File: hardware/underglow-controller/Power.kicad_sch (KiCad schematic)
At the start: 17 parts, among them Q6 Q_PMOS_GDS, U8 ADP2303ARDZ-3.3

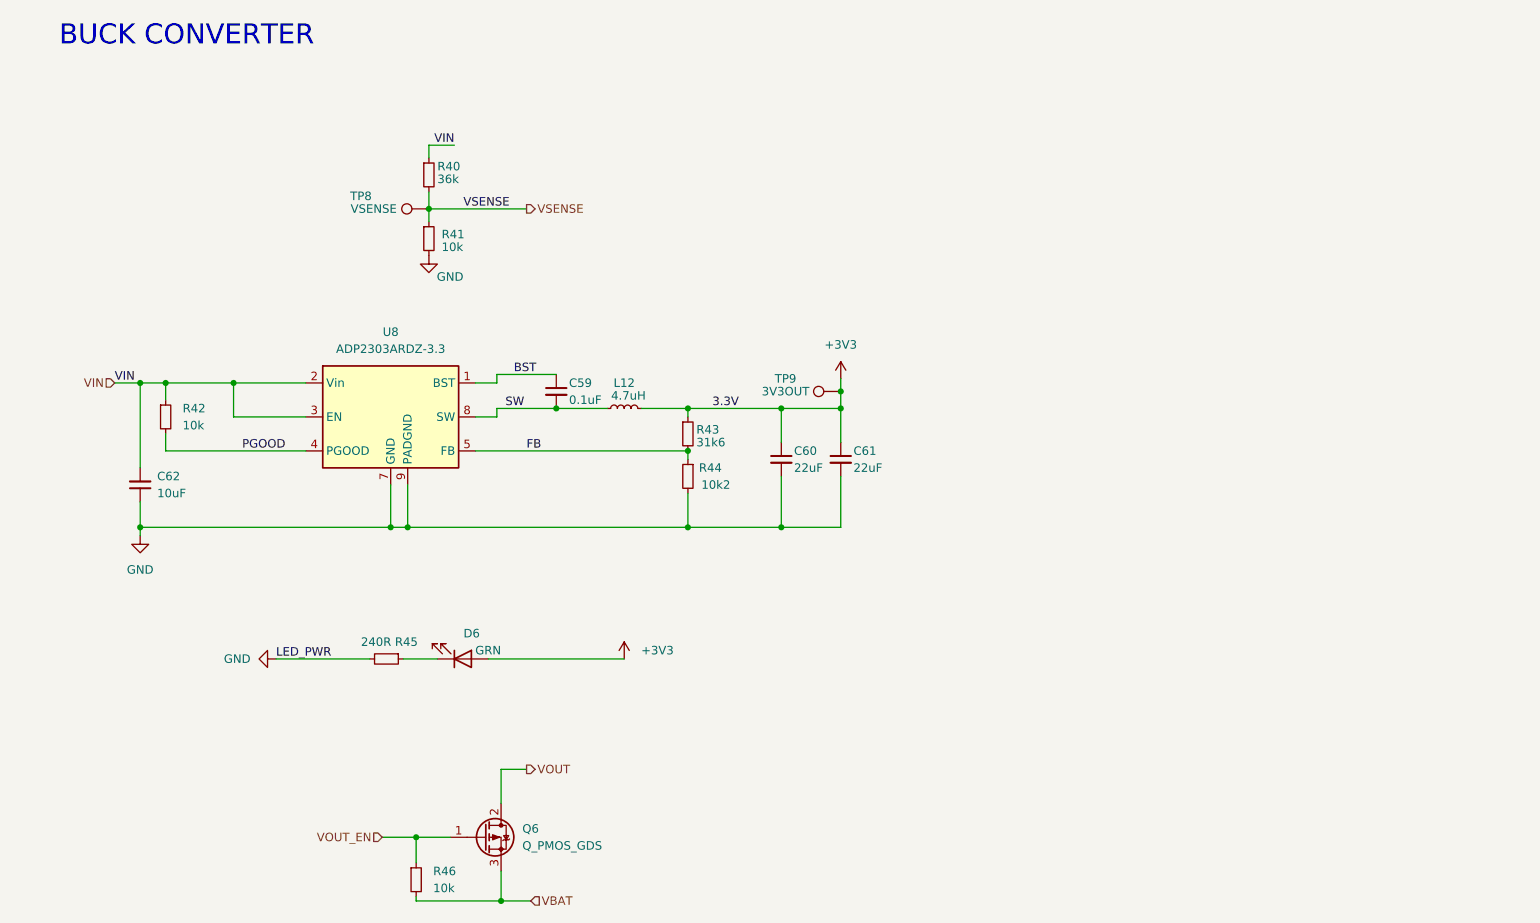
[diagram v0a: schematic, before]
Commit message: replace pmic
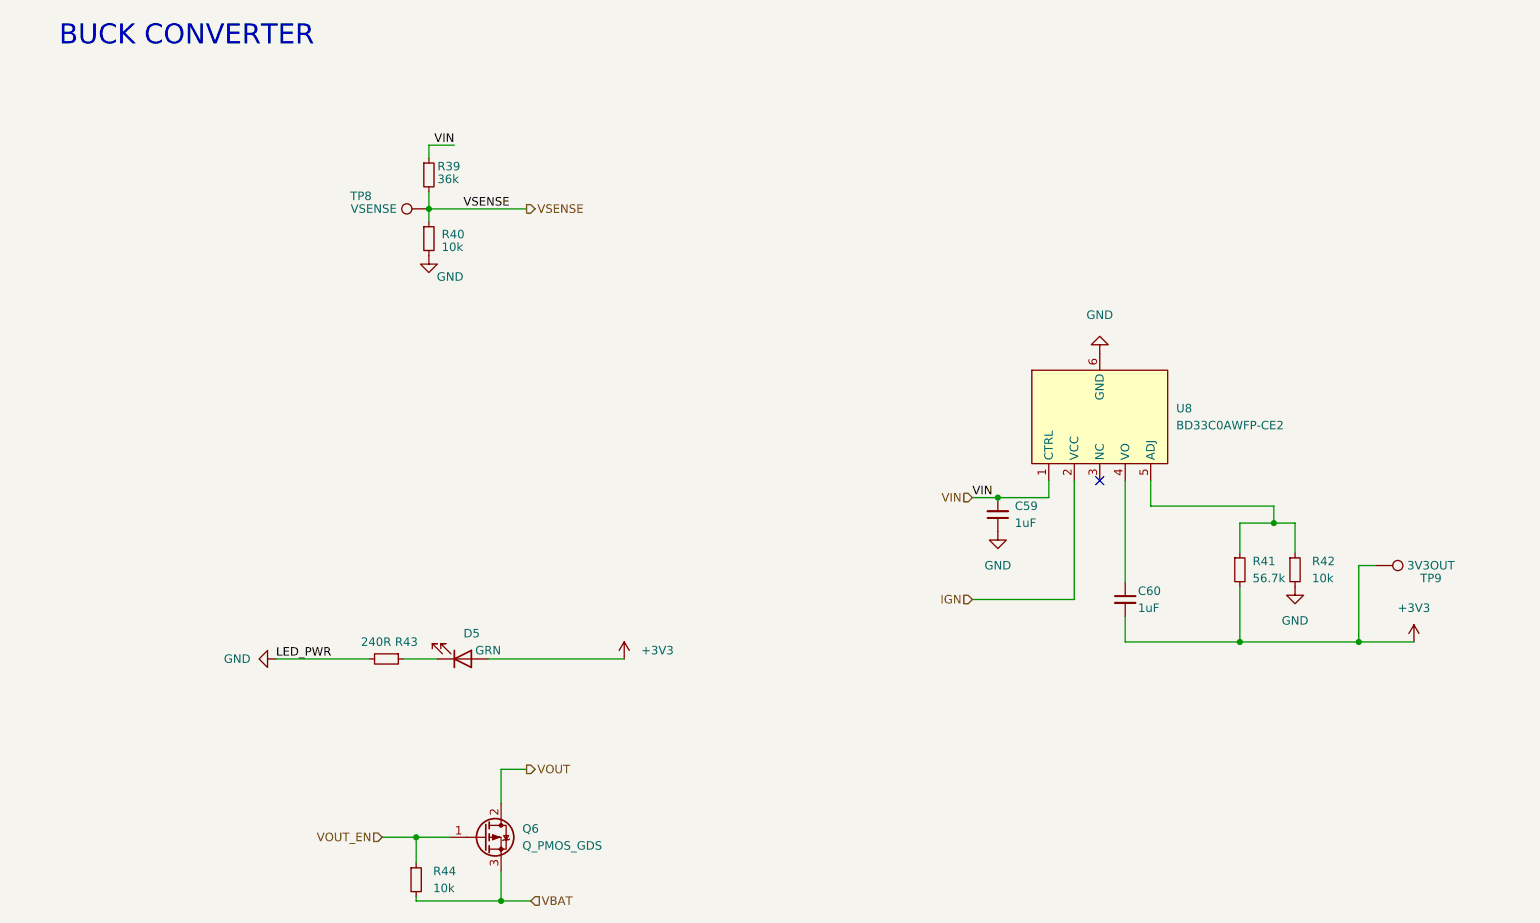
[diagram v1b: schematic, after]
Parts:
- removed C59: 0.1uF, Capacitor_SMD:C_0805_2012Metric, symbol Device:C_Small
- removed C61: 22uF, Capacitor_SMD:C_0805_2012Metric, symbol Device:C_Small
- removed L12: 4.7uH, Inductor_SMD:L_Bourns-SRN6028, symbol Device:L_Small
- removed R43: 31k6, Resistor_SMD:R_0603_1608Metric, symbol Device:R_Small
- removed R44: 10k2, Resistor_SMD:R_0603_1608Metric, symbol Device:R_Small
- removed U8: ADP2303ARDZ-3.3, Package_SO:SOIC-8-1EP_3.9x4.9mm_P1.27mm_EP2.29x3mm_ThermalVias, symbol Regulator_Switching:ADP2303ARDZ-3.3
- added R41: 56.7k, Resistor_SMD:R_0805_2012Metric, symbol Device:R_Small
- added U8: BD33C0AWFP-CE2, Package_TO_SOT_SMD:TO-252-5_TabPin6, symbol ConeCodes:BD33C0AWFP-CE2
- C59: renamed from C62; value 10uF -> 1uF; MPN CL21A106KAFN3NE -> (none)
- C60: value 22uF -> 1uF; MPN CL21A226MOQNNNE -> (none)
- R42: footprint Resistor_SMD:R_0603_1608Metric -> Resistor_SMD:R_0805_2012Metric; MPN RNCP0603FTD10K0 -> (none)
- renumbered D6 to D5, R40 to R39, R41 to R40, R45 to R43, R46 to R44
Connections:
- net PGOOD is gone; now on net GND: R42.2
- net +3V3: now also C60.2, R41.2; no longer C60.1
- net GND: now also U8.6 (GND); no longer C60.2
- net VIN: now also U8.1 (CTRL); no longer R42.1
- new net: R41.1, R42.1, U8.5 (ADJ)
- new net: C60.1, U8.4 (VO)
- new net IGN: U8.2 (VCC)
- no-connect marks 0 -> 1
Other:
- moved on the sheet: C59, TP9

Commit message: iasdf
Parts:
- removed Q6: Q_PMOS_GDS, Package_TO_SOT_SMD:TO-252-2, symbol Device:Q_PMOS_GDS
- removed R44: 10k, Resistor_SMD:R_0603_1608Metric, symbol Device:R_Small
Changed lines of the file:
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@@
   (junction (at 198.755 92.075) (diameter 0) (color 0 0 0 0)
-  )
-  (junction (at 70.485 139.065) (diameter 0) (color 0 0 0 0)
-  )
-  (junction (at 83.185 148.59) (diameter 0) (color 0 0 0 0)
   )
   (junction (at 193.675 109.855) (diameter 0) (color 0 0 0 0)
@@
     (stroke (width 0) (type default) (color 0 0 0 0))
   )
-  (wire (pts (xy 87.63 148.59) (xy 83.185 148.59))
-    (stroke (width 0) (type default) (color 0 0 0 0))
-  )
   (wire (pts (xy 176.53 109.855) (xy 176.53 106.045))
     (stroke (width 0) (type default) (color 0 0 0 0))
   )
-  (wire (pts (xy 83.185 148.59) (xy 83.185 144.145))
-    (stroke (width 0) (type default) (color 0 0 0 0))
-  )
-  (wire (pts (xy 70.485 139.065) (xy 70.485 142.875))
-    (stroke (width 0) (type default) (color 0 0 0 0))
-  )
   (wire (pts (xy 213.995 98.425) (xy 211.455 98.425))
     (stroke (width 0) (type default) (color 0 0 0 0))
@@
     (stroke (width 0) (type default) (color 0 0 0 0))
   )
-  (wire (pts (xy 65.405 139.065) (xy 70.485 139.065))
-    (stroke (width 0) (type default) (color 0 0 0 0))
-  )
   (wire (pts (xy 193.675 92.075) (xy 198.755 92.075))
     (stroke (width 0) (type default) (color 0 0 0 0))
@@
     (stroke (width 0) (type default) (color 0 0 0 0))
   )
-  (wire (pts (xy 70.485 139.065) (xy 75.565 139.065))
-    (stroke (width 0) (type default) (color 0 0 0 0))
-  )
   (wire (pts (xy 176.53 85.725) (xy 176.53 100.965))
     (stroke (width 0) (type default) (color 0 0 0 0))
@@
     (stroke (width 0) (type default) (color 0 0 0 0))
   )
-  (wire (pts (xy 83.185 128.905) (xy 83.185 133.985))
-    (stroke (width 0) (type default) (color 0 0 0 0))
-  )
   (wire (pts (xy 211.455 98.425) (xy 211.455 109.855))
     (stroke (width 0) (type default) (color 0 0 0 0))
@@
     (stroke (width 0) (type default) (color 0 0 0 0))
   )
-  (wire (pts (xy 70.485 148.59) (xy 70.485 147.955))
-    (stroke (width 0) (type default) (color 0 0 0 0))
-  )
-  (wire (pts (xy 83.185 148.59) (xy 70.485 148.59))
-    (stroke (width 0) (type default) (color 0 0 0 0))
-  )
   (wire (pts (xy 180.34 85.725) (xy 180.34 89.535))
-    (stroke (width 0) (type default) (color 0 0 0 0))
-  )
-  (wire (pts (xy 86.995 128.905) (xy 83.185 128.905))
     (stroke (width 0) (type default) (color 0 0 0 0))
   )
@@
     (effects (font (size 1.27 1.27)) (justify left))
   )
-  (hierarchical_label "VBAT" (shape input) (at 87.63 148.59 0)
-    (effects (font (size 1.27 1.27)) (justify left))
-  )
   (hierarchical_label "VIN" (shape input) (at 153.67 88.265 180)
     (effects (font (size 1.27 1.27)) (justify right))
-  )
-  (hierarchical_label "VOUT_EN" (shape input) (at 65.405 139.065 180)
-    (effects (font (size 1.27 1.27)) (justify right))
-  )
-  (hierarchical_label "VOUT" (shape output) (at 86.995 128.905 0)
-    (effects (font (size 1.27 1.27)) (justify left))
   )
   (symbol (lib_id "power:GND") (at 201.93 101.6 0) (unit 1)
@@
       (effects (font (size 1.27 1.27)) hide)
     )
-    (pin "1")
-    (pin "2")
-  )
-  (symbol (lib_id "Device:Q_PMOS_GDS") (at 80.645 139.065 0) (unit 1)
-    (in_bom yes) (on_board yes) (fields_autoplaced)
-    (property "Reference" "Q6" (id 0) (at 86.36 137.7949 0)
-      (effects (font (size 1.27 1.27)) (justify left))
-    )
-    (property "Value" "Q_PMOS_GDS" (id 1) (at 86.36 140.3349 0)
-      (effects (font (size 1.27 1.27)) (justify left))
-    )
-    (property "Footprint" "Package_TO_SOT_SMD:TO-252-2" (id 2) (at 85.725 136.525 0)
-      (effects (font (size 1.27 1.27)) hide)
-    )
-    (property "Datasheet" "~" (id 3) (at 80.645 139.065 0)
-      (effects (font (size 1.27 1.27)) hide)
-    )
-    (property "MPN" "STD15P6F6AG" (id 4) (at 80.645 139.065 0)
-      (effects (font (size 1.27 1.27)) hide)
-    )
-    (property "Description" "MOSFET P-CH 60V 10A DPAK" (id 5) (at 80.645 139.065 0)
-      (effects (font (size 1.27 1.27)) hide)
-    )
-    (pin "1")
-    (pin "2")
-    (pin "3")
-  )
-  (symbol (lib_id "Device:R_Small") (at 70.485 145.415 0) (unit 1)
-    (in_bom yes) (on_board yes) (fields_autoplaced)
-    (property "Reference" "R44" (id 0) (at 73.025 144.1449 0)
-      (effects (font (size 1.27 1.27)) (justify left))
-    )
-    (property "Value" "10k" (id 1) (at 73.025 146.6849 0)
-      (effects (font (size 1.27 1.27)) (justify left))
-    )
-    (property "Footprint" "Resistor_SMD:R_0603_1608Metric" (id 2) (at 70.485 145.415 0)
-      (effects (font (size 1.27 1.27)) hide)
-    )
-    (property "Datasheet" "~" (id 3) (at 70.485 145.415 0)
-      (effects (font (size 1.27 1.27)) hide)
-    )
-    (property "MPN" "RNCP0603FTD10K0" (id 5) (at 70.485 145.415 0)
-      (effects (font (size 1.27 1.27)) hide)
-    )
-    (property "Description" "RES 10K OHM 1% 1/8W 0603" (id 6) (at 70.485 145.415 0)
-      (effects (font (size 1.27 1.27)) hide)
-    )

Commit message: schematic rework progress
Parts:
- renumbered C59 to C57, C60 to C58, D5 to D4, R39 to R40, R40 to R41, R41 to R42, R42 to R43, R43 to R44, U8 to U6
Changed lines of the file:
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@@
   (symbol (lib_id "power:GND") (at 201.93 101.6 0) (unit 1)
     (in_bom yes) (on_board yes) (fields_autoplaced)
-    (property "Reference" "#PWR084" (id 0) (at 201.93 107.95 0)
+    (property "Reference" "#PWR075" (id 0) (at 201.93 107.95 0)
       (effects (font (size 1.27 1.27)) hide)
     )
@@
   (symbol (lib_id "power:+3V3") (at 219.71 109.855 0) (unit 1)
     (in_bom yes) (on_board yes) (fields_autoplaced)
-    (property "Reference" "#PWR085" (id 0) (at 219.71 113.665 0)
+    (property "Reference" "#PWR076" (id 0) (at 219.71 113.665 0)
       (effects (font (size 1.27 1.27)) hide)
     )
@@
   (symbol (lib_id "power:GND") (at 49.53 112.395 270) (unit 1)
     (in_bom yes) (on_board yes) (fields_autoplaced)
-    (property "Reference" "#PWR086" (id 0) (at 43.18 112.395 0)
+    (property "Reference" "#PWR077" (id 0) (at 43.18 112.395 0)
       (effects (font (size 1.27 1.27)) hide)
     )
@@
   (symbol (lib_id "Device:R_Small") (at 72.39 40.005 0) (unit 1)
     (in_bom yes) (on_board yes)
-    (property "Reference" "R39" (id 0) (at 73.66 38.735 0)
+    (property "Reference" "R40" (id 0) (at 73.66 38.735 0)
       (effects (font (size 1.27 1.27)) (justify left))
     )
@@
   (symbol (lib_id "Device:C_Small") (at 157.48 90.805 180) (unit 1)
     (in_bom yes) (on_board yes)
-    (property "Reference" "C59" (id 0) (at 160.02 89.5285 0)
+    (property "Reference" "C57" (id 0) (at 160.02 89.5285 0)
       (effects (font (size 1.27 1.27)) (justify right))
     )
@@
   (symbol (lib_id "Device:R_Small") (at 193.675 99.06 0) (unit 1)
     (in_bom yes) (on_board yes) (fields_autoplaced)
-    (property "Reference" "R41" (id 0) (at 195.58 97.7899 0)
+    (property "Reference" "R42" (id 0) (at 195.58 97.7899 0)
       (effects (font (size 1.27 1.27)) (justify left))
     )
@@
   (symbol (lib_id "ConeCodes:BD33C0AWFP-CE2") (at 172.72 78.105 0) (unit 1)
     (in_bom yes) (on_board yes) (fields_autoplaced)
-    (property "Reference" "U8" (id 0) (at 184.15 74.9299 0)
+    (property "Reference" "U6" (id 0) (at 184.15 74.9299 0)
       (effects (font (size 1.27 1.27)) (justify left))
     )
@@
   (symbol (lib_id "power:GND") (at 157.48 93.345 0) (unit 1)
     (in_bom yes) (on_board yes) (fields_autoplaced)
-    (property "Reference" "#PWR083" (id 0) (at 157.48 99.695 0)
+    (property "Reference" "#PWR074" (id 0) (at 157.48 99.695 0)
       (effects (font (size 1.27 1.27)) hide)
     )
@@
   (symbol (lib_id "Device:C_Small") (at 176.53 103.505 0) (unit 1)
     (in_bom yes) (on_board yes)
-    (property "Reference" "C60" (id 0) (at 178.435 102.2412 0)
+    (property "Reference" "C58" (id 0) (at 178.435 102.2412 0)
       (effects (font (size 1.27 1.27)) (justify left))
     )
@@
   (symbol (lib_id "Device:LED") (at 77.47 112.395 0) (mirror x) (unit 1)
     (in_bom yes) (on_board yes)
-    (property "Reference" "D5" (id 0) (at 80.01 108.585 0)
+    (property "Reference" "D4" (id 0) (at 80.01 108.585 0)
       (effects (font (size 1.27 1.27)) (justify right))
     )
@@
   (symbol (lib_id "Device:R_Small") (at 66.04 112.395 270) (unit 1)
     (in_bom yes) (on_board yes)
-    (property "Reference" "R43" (id 0) (at 67.31 109.855 90)
+    (property "Reference" "R44" (id 0) (at 67.31 109.855 90)
       (effects (font (size 1.27 1.27)) (justify left))
     )
@@
   (symbol (lib_id "Device:R_Small") (at 72.39 49.53 0) (unit 1)
     (in_bom yes) (on_board yes)
-    (property "Reference" "R40" (id 0) (at 74.295 48.895 0)
+    (property "Reference" "R41" (id 0) (at 74.295 48.895 0)
       (effects (font (size 1.27 1.27)) (justify left))
     )
@@
   (symbol (lib_id "power:GND") (at 72.39 52.07 0) (unit 1)
     (in_bom yes) (on_board yes)
-    (property "Reference" "#PWR081" (id 0) (at 72.39 58.42 0)
+    (property "Reference" "#PWR072" (id 0) (at 72.39 58.42 0)
       (effects (font (size 1.27 1.27)) hide)
     )
@@
   (symbol (lib_id "power:+3V3") (at 101.6 112.395 0) (unit 1)
     (in_bom yes) (on_board yes) (fields_autoplaced)
-    (property "Reference" "#PWR087" (id 0) (at 101.6 116.205 0)
+    (property "Reference" "#PWR078" (id 0) (at 101.6 116.205 0)
       (effects (font (size 1.27 1.27)) hide)
     )
@@
   (symbol (lib_id "power:GND") (at 172.72 66.675 180) (unit 1)
     (in_bom yes) (on_board yes) (fields_autoplaced)
-    (property "Reference" "#PWR082" (id 0) (at 172.72 60.325 0)
+    (property "Reference" "#PWR073" (id 0) (at 172.72 60.325 0)
       (effects (font (size 1.27 1.27)) hide)
     )
@@
   (symbol (lib_id "Device:R_Small") (at 201.93 99.06 0) (unit 1)
     (in_bom yes) (on_board yes) (fields_autoplaced)
-    (property "Reference" "R42" (id 0) (at 204.47 97.7899 0)
-      (effects (font (size 1.27 1.27)) (justify left))
-    )
+    (property "Reference" "R43" (id 0) (at 204.47 97.7899 0)
+      (effects (font (size 1.27 1.27)) (justify left))
+    )

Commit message: schematic almost done
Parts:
- added D?: D_Schottky_Small, Diode_SMD:D_SMA, symbol Device:D_Schottky_Small
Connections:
- net GND: now also D?.2 (A)
- net IGN renamed VBATT
- net VBATT: now also C57.2, R40.1, D?.1 (K)
- removed net VIN: C57.2, R40.1, U6.1 (CTRL)
- new net IGNITION: U6.1 (CTRL)
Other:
- moved on the sheet: C57, C58, D4, R40, R41, R42, R43, R44, TP8, TP9, U6
